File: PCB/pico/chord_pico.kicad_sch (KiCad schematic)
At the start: 83 parts, among them SW1 SW_DIP_x01, SW2 SW_DIP_x01, U1 PiPico, U2 ADG706BRUZ, U6 LM4040DBZ-3, U7 TPS7A2042

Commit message: PCB progress 60%
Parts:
- removed JP2: Bypass, Jumper:SolderJumper-2_P1.3mm_Open_RoundedPad1.0x1.5mm, symbol Jumper:SolderJumper_2_Open
- added C19, C20, C21, C22, C23, C24, C25, C26, C27, C28: 0.1uF, Capacitor_SMD:C_0603_1608Metric_Pad1.08x0.95mm_HandSolder, symbol Device:C
- renumbered C19 to CC1, C20 to CC2, H4 to H1, H6 to H2, H2 to H4, H1 to H5, H5 to H6
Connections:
- net V1 is gone; now on net Vref: C8.1
- net V2 is gone; now on net Vref: C9.1
- net +5V: now also C19.1, C20.1, C21.1, C22.1, C23.1, C24.1, C25.1, C26.1, C27.1, C28.1; no longer C10.1, C11.1, C12.1, C13.1, C14.1, C15.1, C16.1
- net AUX1: now also U1.19 (GPIO14); no longer U1.1 (GPIO0)
- net AUX2: now also U1.20 (GPIO15); no longer U1.2 (GPIO1)
- net F1: now also U2.25 (S7); no longer U2.7 (S13)
- net F2: now also U2.26 (S8)
- net F3: now also U2.4 (S16); no longer U2.5 (S15)
- net F4: now also U2.5 (S15)
- net GND: now also H13.3 (G), H14.3 (G), H15.3 (G), H16.3 (G), SW1.2, SW2.2, C19.2, C20.2, C21.2, C22.2, C23.2, C24.2, C25.2, C26.2, C27.2, C28.2
- net K1: now also H1.2 (OUT), U2.24 (S6); no longer H6.2 (OUT), U2.19 (S1)
- net K10: now also U2.8 (S12); no longer U2.10 (S10)
- net K11: now also U2.7 (S13); no longer U2.9 (S11)
- net K12: now also U2.6 (S14); no longer U2.8 (S12)
- net K2: now also H2.2 (OUT), U2.23 (S5); no longer H5.2 (OUT), U2.20 (S2)
- net K3: now also H3.2 (OUT), U2.22 (S4); no longer H4.2 (OUT), U2.21 (S3)
- net K4: now also H4.2 (OUT), U2.21 (S3); no longer H3.2 (OUT), U2.22 (S4)
- net K5: now also H5.2 (OUT), U2.20 (S2); no longer H2.2 (OUT), U2.23 (S5)
- net K6: now also H6.2 (OUT), U2.19 (S1); no longer H1.2 (OUT), U2.24 (S6)
- net K7: now also U2.11 (S9); no longer U2.25 (S7)
- net K8: now also U2.10 (S10); no longer U2.26 (S8)
- net K9: now also U2.9 (S11); no longer U2.11 (S9)
- net Vref: now also C10.1, C11.1, C12.1, C13.1, C14.1, C15.1, C16.1
- net at D1.I (In), D13.I (In), D14.I (In)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: now also U1.1 (GPIO0); no longer U1.17 (GPIO13)
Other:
- moved on the sheet: C1, C2, C3, C4, C5, C6, C7, CC1, CC2, D1, D10, D11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

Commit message: PCB v1.0
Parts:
- added CC3: 0.1uF, Capacitor_SMD:C_0603_1608Metric_Pad1.08x0.95mm_HandSolder, symbol Device:C
- R4: value 10K -> 5.1K
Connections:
- net GND: now also CC3.2
- net Vref: now also CC3.1
- net at U1.22 (GPIO17): now also U2.14 (A3); no longer U2.18 (EN)
- net at U1.24 (GPIO18): now also U2.15 (A2); no longer U2.14 (A3)
- net at U1.25 (GPIO19): now also U2.16 (A1); no longer U2.15 (A2)
- net at U1.26 (GPIO20): now also U2.17 (A0); no longer U2.16 (A1)
- net at U1.27 (GPIO21): now also U2.18 (EN); no longer U2.17 (A0)
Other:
- moved on the sheet: R3, Z1

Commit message: PCB v1.11
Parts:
- removed C13, C14, C15, C16: 0.1uF, Capacitor_SMD:C_0603_1608Metric_Pad1.08x0.95mm_HandSolder, symbol Device:C
- removed H13, H14, H15, H16: SS49E_SOT23, Package_TO_SOT_THT:TO-92Flat, symbol nos_plus:SS49E_SOT23
- added C29, C30, C31, C32: 0.1uF, Capacitor_SMD:C_0603_1608Metric_Pad1.08x0.95mm_HandSolder, symbol Device:C
- added D35, D36, D37, D38, D39, D40, D41, D42: WS2812B_Unified, chord_pico:WS2812B-2835, symbol chord_pico:WS2812B_Unified
- added IR1, IR10, IR2, IR3, IR4, IR5, IR6, IR7, IR8, IR9: ITR1502, chord_pico:ITR1502, symbol chord_pico:ITR1502
- added R10, R12, R14, R16, R18, R20, R22, R24, R6, R8: 10K, Resistor_SMD:R_0603_1608Metric_Pad0.98x0.95mm_HandSolder, symbol Device:R
- added R11, R13, R15, R17, R19, R21, R23, R5, R7, R9: 200, Resistor_SMD:R_0603_1608Metric_Pad0.98x0.95mm_HandSolder, symbol Device:R
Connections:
- net +5V: now also C29.1, C30.1, C31.1, C32.1, D35.V (VDD), D36.V (VDD), D37.V (VDD), D38.V (VDD), D39.V (VDD), D40.V (VDD), D41.V (VDD), D42.V (VDD)
- net F1: now also U1.4 (GPIO2), IR1.1, R6.2; no longer U2.25 (S7)
- net F2: now also U1.5 (GPIO3), IR2.1, R8.2; no longer U2.26 (S8)
- net F3: now also U1.6 (GPIO4), IR3.1, R10.2; no longer U2.4 (S16)
- net F4: now also U1.7 (GPIO5), IR4.1, R12.2; no longer U2.5 (S15)
- net GND: now also C29.2, C30.2, C31.2, C32.2, D35.G (VSS), D36.G (VSS), D37.G (VSS), D38.G (VSS), D39.G (VSS), D40.G (VSS), D41.G (VSS), D42.G (VSS), R10.1, R11.1, R12.1, R13.1, R14.1, R15.1, R16.1, R17.1, R18.1, R19.1, R20.1, R21.1, R22.1, R23.1, R24.1, R5.1, R6.1, R7.1, R8.1, R9.1
- net F6: now reaches U1.10 (GPIO7)
- net F6: now also IR6.1, R16.2
- net F7: now reaches U1.11 (GPIO8)
- net F7: now also IR7.1, R18.2
- net F8: now reaches U1.12 (GPIO9)
- net F8: now also IR8.1, R20.2
- net F9: now reaches U1.14 (GPIO10)
- net F9: now also IR9.1, R22.2
- net F10: now reaches U1.15 (GPIO11)
- net F10: now also IR10.1, R24.2
- net at U1.2 (GPIO1): now also D35.I (In), D39.I (In)
- net +3.3V: now reaches U1.36 (3V3)
- net +3.3V: now also IR1.2, IR1.4 (A), IR10.2, IR10.4 (A), IR2.2, IR2.4 (A), IR3.2, IR3.4 (A), IR4.2, IR4.4 (A), IR5.2, IR5.4 (A), IR6.2, IR6.4 (A), IR7.2, IR7.4 (A), IR8.2, IR8.4 (A), IR9.2, IR9.4 (A)
- net F5: now reaches U1.9 (GPIO6)
- net F5: now also IR5.1, R14.2
- new net: D36.O (Out), D37.I (In), D41.I (In)
- new net: D37.O (Out), D38.I (In), D42.I (In)
- new net: IR6.3 (K), R15.2
- new net: D35.O (Out), D36.I (In), D40.I (In)
- new net: IR5.3 (K), R13.2
- new net: IR7.3 (K), R17.2
- new net: IR8.3 (K), R19.2
- new net: IR2.3 (K), R7.2
- new net: IR4.3 (K), R11.2
- new net: IR10.3 (K), R23.2
- new net: IR1.3 (K), R5.2
- new net: IR3.3 (K), R9.2
- new net: IR9.3 (K), R21.2
- no-connect marks 41 -> 36
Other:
- moved on the sheet: CC3, D1, D10, D11, D12, D13, D14, D15, D16, D17, D18, D19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

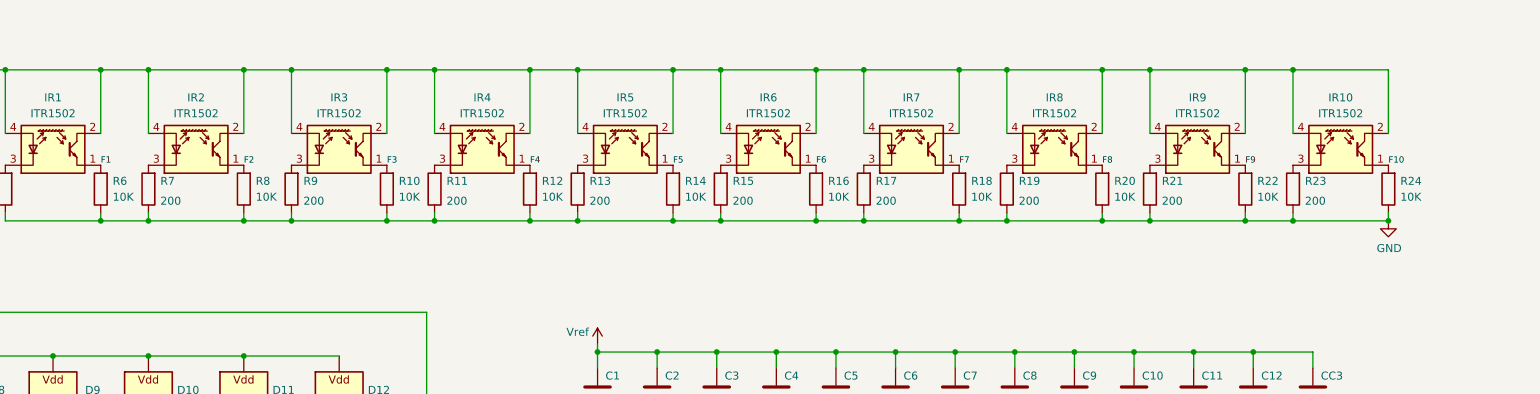
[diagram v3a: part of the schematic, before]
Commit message: PCB v1.2 (correct values and signature)
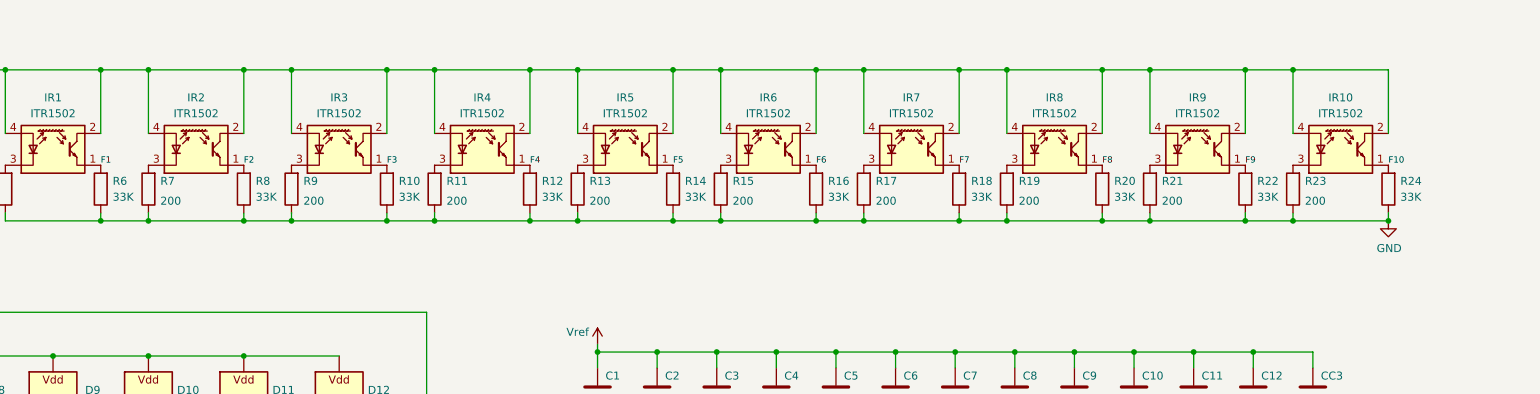
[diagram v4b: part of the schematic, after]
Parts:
- R10, R12, R14, R16, R18, R20, R22, R24, R6, R8: value 10K -> 33K
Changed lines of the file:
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@@
 			)
 		)
-		(property "Value" "10K"
+		(property "Value" "33K"
 			(at 216.535 170.815 0)
 			(effects
@@
 			)
 		)
-		(property "Value" "10K"
+		(property "Value" "33K"
 			(at 239.395 170.815 0)
 			(effects
@@
 			)
 		)
-		(property "Value" "10K"
+		(property "Value" "33K"
 			(at 330.835 170.815 0)
 			(effects
@@
 			)
 		)
-		(property "Value" "10K"
+		(property "Value" "33K"
 			(at 376.555 170.815 0)
 			(effects
@@
 			)
 		)
-		(property "Value" "10K"
+		(property "Value" "33K"
 			(at 353.695 170.815 0)
 			(effects
@@
 			)
 		)
-		(property "Value" "10K"
+		(property "Value" "33K"
 			(at 262.255 170.815 0)
 			(effects
@@
 			)
 		)
-		(property "Value" "10K"
+		(property "Value" "33K"
 			(at 193.675 170.815 0)
 			(effects
@@
 			)
 		)
-		(property "Value" "10K"
+		(property "Value" "33K"
 			(at 285.115 170.815 0)
 			(effects
@@
 			)
 		)
-		(property "Value" "10K"
+		(property "Value" "33K"
 			(at 170.815 170.815 0)
 			(effects
@@
 			)
 		)
-		(property "Value" "10K"
+		(property "Value" "33K"
 			(at 307.975 170.815 0)
 			(effects

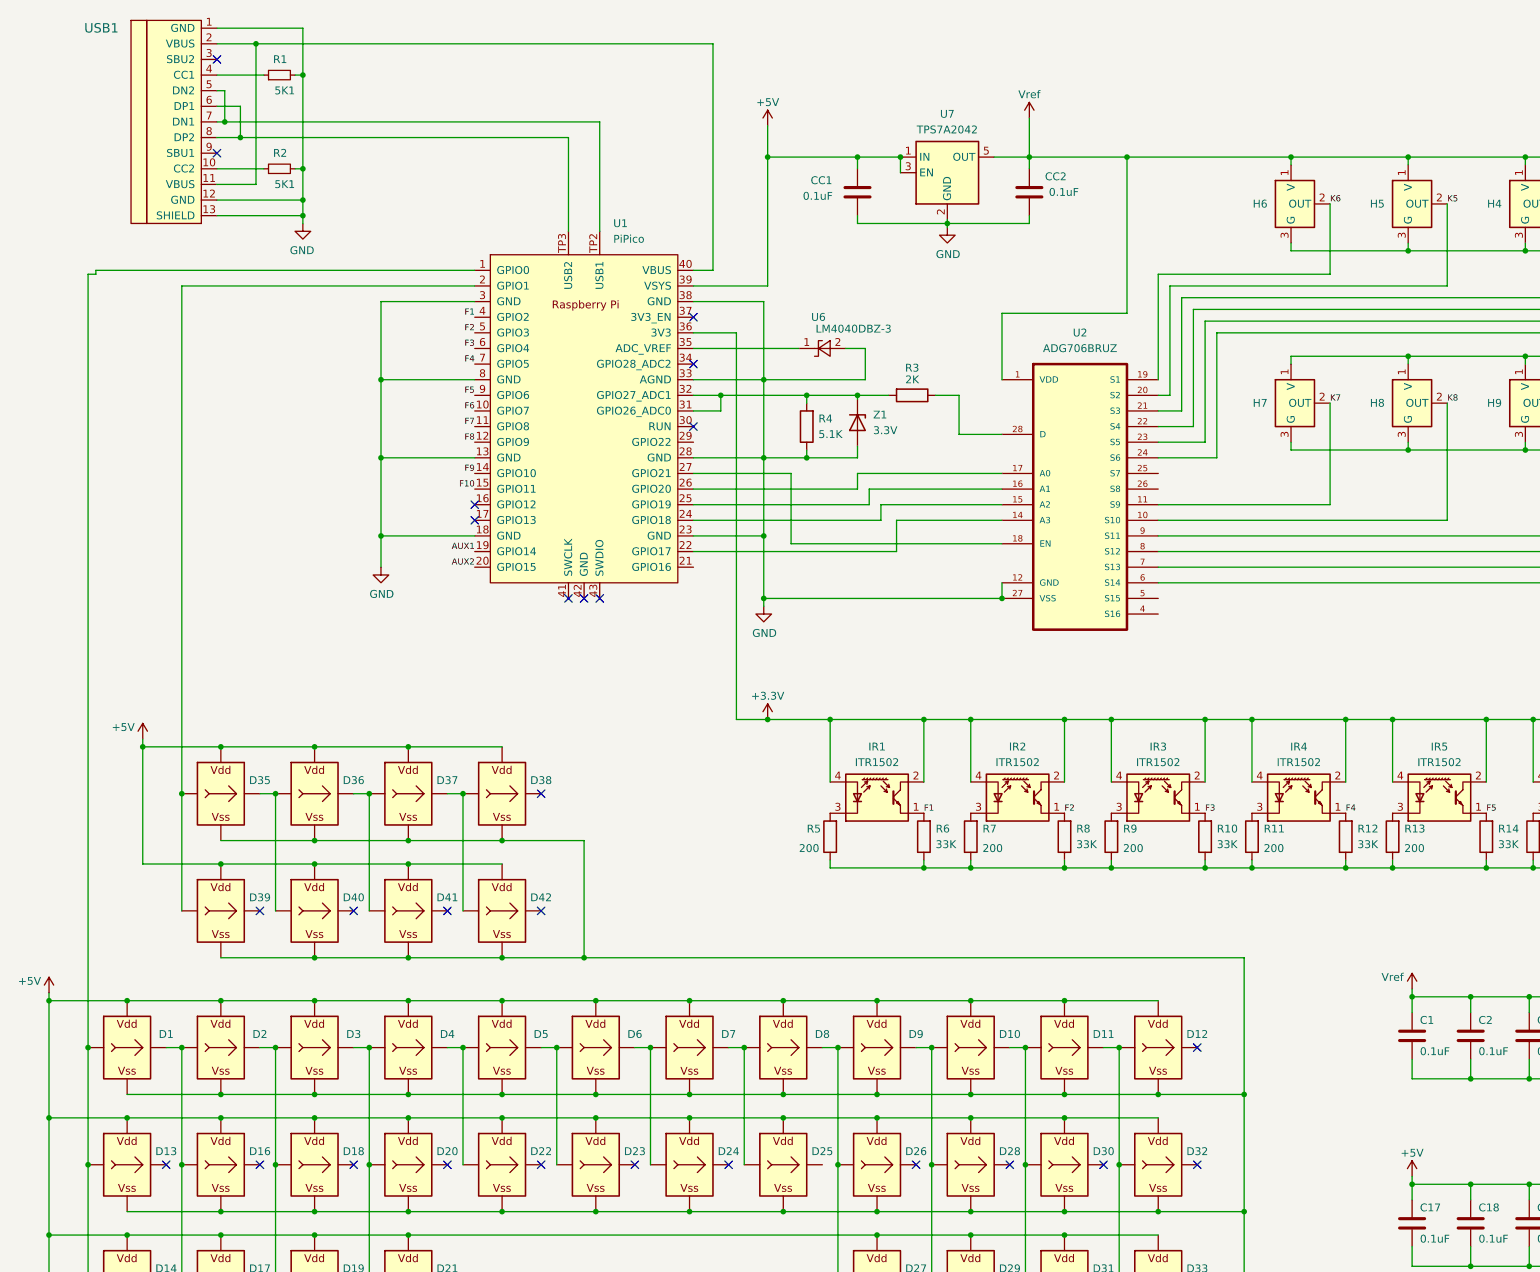
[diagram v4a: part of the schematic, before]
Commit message: PCB optimization, VBUS for LDO
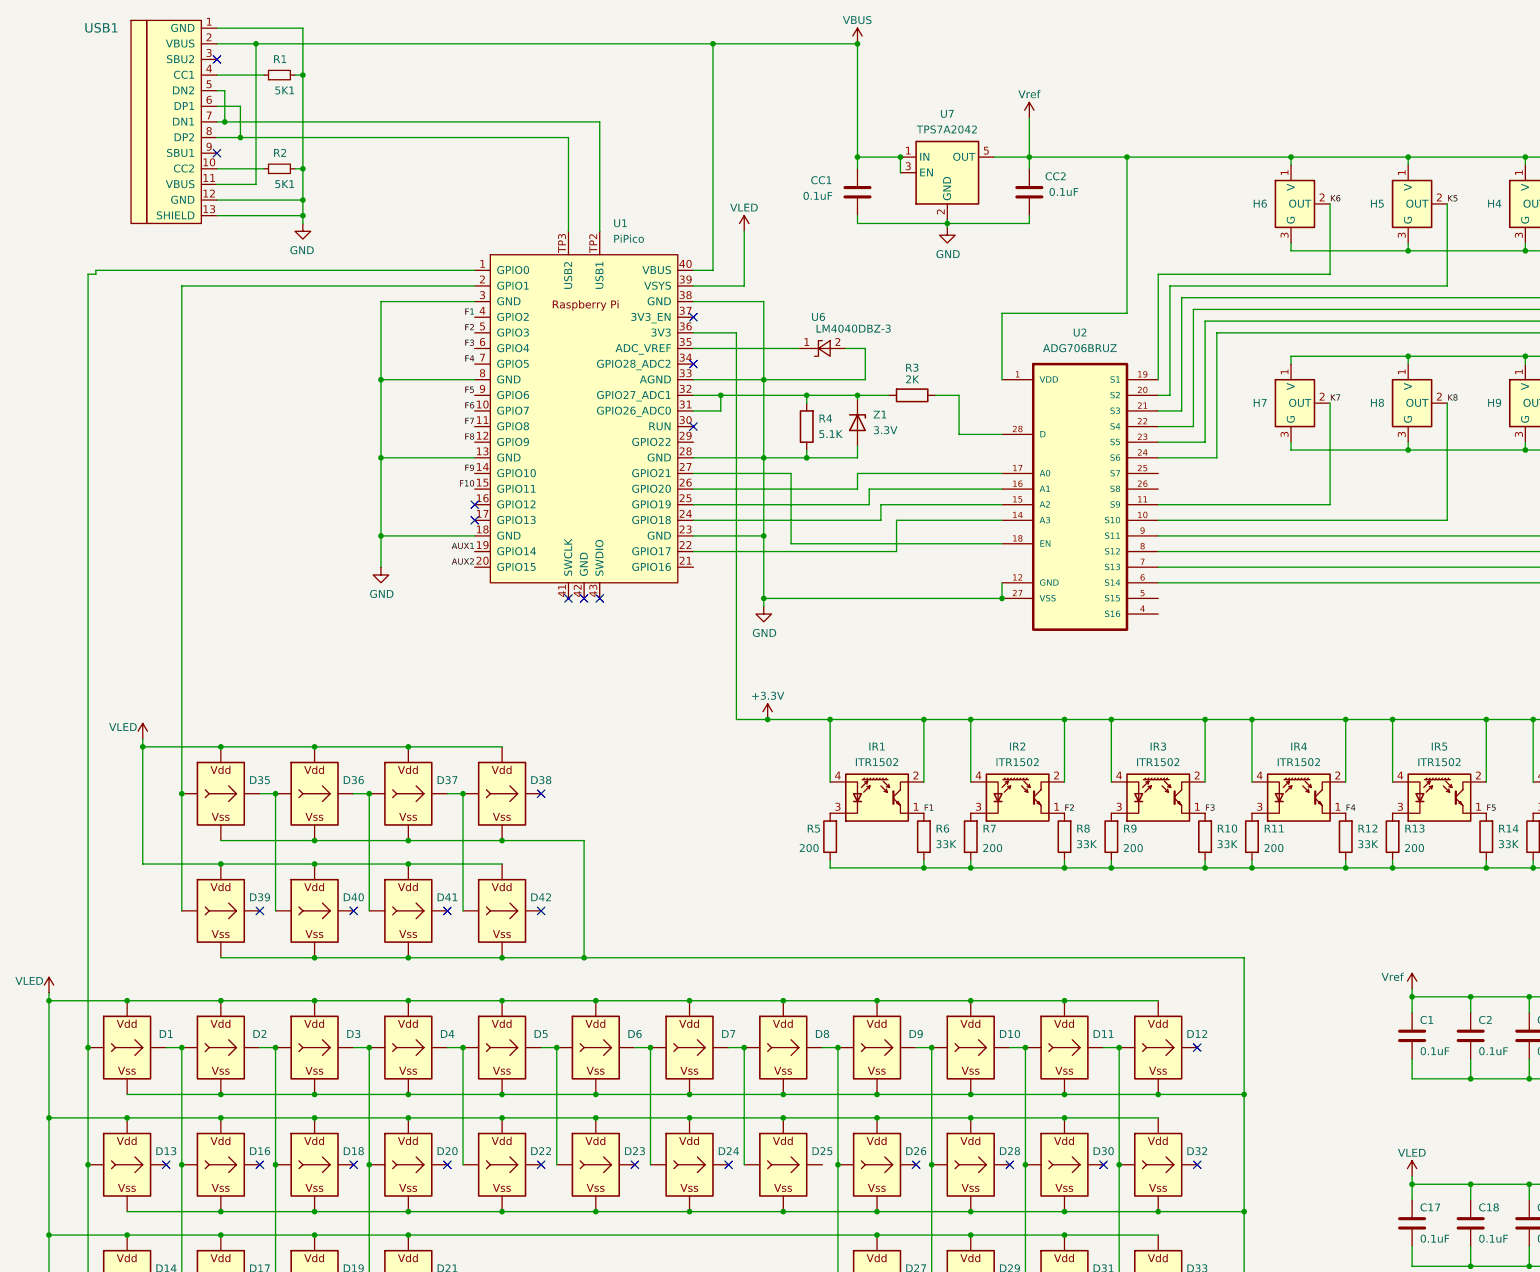
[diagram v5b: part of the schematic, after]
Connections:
- net VBUS: now reaches U1.40 (VBUS), USB1.11 (VBUS), USB1.2 (VBUS)
- net VBUS: now also CC1.1, U7.1 (IN), U7.3 (EN)
- net +5V renamed VLED
- net VLED: no longer CC1.1, U7.1 (IN), U7.3 (EN)
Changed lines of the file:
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@@
 	)
 	(junction
-		(at 143.51 59.055)
-		(diameter 0)
-		(color 0 0 0 0)
-	)
-	(junction
 		(at 295.91 208.915)
 		(diameter 0)
@@
 	)
 	(junction
+		(at 134.62 40.64)
+		(diameter 0)
+		(color 0 0 0 0)
+	)
+	(junction
 		(at 165.1 59.055)
 		(diameter 0)
@@
 	)
 	(junction
-		(at 158.115 59.055)
-		(diameter 0)
-		(color 0 0 0 0)
-	)
-	(junction
 		(at 336.55 150.495)
 		(diameter 0)
@@
 	)
 	(junction
+		(at 158.115 59.055)
+		(diameter 0)
+		(color 0 0 0 0)
+	)
+	(junction
 		(at 100.33 189.23)
 		(diameter 0)
@@
 	)
 	(junction
+		(at 158.115 40.64)
+		(diameter 0)
+		(color 0 0 0 0)
+	)
+	(junction
 		(at 248.285 226.06)
 		(diameter 0)
@@
 	(wire
 		(pts
-			(xy 143.51 59.055) (xy 158.115 59.055)
-		)
-		(stroke
-			(width 0)
-			(type default)
-		)
-	)
-	(wire
-		(pts
 			(xy 237.49 174.625) (xy 245.11 174.625)
 		)
@@
 	(wire
 		(pts
-			(xy 143.51 59.055) (xy 143.51 53.975)
+			(xy 139.7 71.12) (xy 139.7 80.01)
 		)
 		(stroke
@@
 	(wire
 		(pts
+			(xy 134.62 40.64) (xy 158.115 40.64)
+		)
+		(stroke
+			(width 0)
+			(type default)
+		)
+	)
+	(wire
+		(pts
 			(xy 266.7 106.68) (xy 285.75 106.68)
 		)
@@
 	(wire
 		(pts
-			(xy 305.435 239.395) (xy 314.96 239.395)
+			(xy 158.115 40.64) (xy 158.115 59.055)
 		)
 		(stroke
@@
 	(wire
 		(pts
-			(xy 91.44 162.56) (xy 93.98 162.56)
+			(xy 305.435 239.395) (xy 314.96 239.395)
 		)
 		(stroke
@@
 	(wire
 		(pts
-			(xy 54.61 154.94) (xy 69.85 154.94)
+			(xy 91.44 162.56) (xy 93.98 162.56)
 		)
 		(stroke
@@
 	(wire
 		(pts
-			(xy 347.345 59.055) (xy 347.345 91.44)
+			(xy 54.61 154.94) (xy 69.85 154.94)
 		)
 		(stroke
-			(width 0.254)
+			(width 0)
 			(type default)
 		)
@@
 	(wire
 		(pts
-			(xy 186.055 59.055) (xy 186.055 60.96)
+			(xy 347.345 59.055) (xy 347.345 91.44)
 		)
 		(stroke
@@
 	(wire
 		(pts
-			(xy 176.53 150.495) (xy 191.77 150.495)
+			(xy 186.055 59.055) (xy 186.055 60.96)
 		)
 		(stroke
-			(width 0)
+			(width 0.254)
 			(type default)
 		)
@@
 	(wire
 		(pts
-			(xy 143.51 80.01) (xy 143.51 59.055)
+			(xy 176.53 150.495) (xy 191.77 150.495)
 		)
 		(stroke
@@
 	(wire
 		(pts
-			(xy 131.445 80.01) (xy 143.51 80.01)
+			(xy 131.445 80.01) (xy 139.7 80.01)
 		)
 		(stroke
@@
 	)
 	(symbol
+		(lib_id "power:+5V")
+		(at 158.115 40.64 0)
+		(unit 1)
+		(exclude_from_sim no)
+		(in_bom yes)
+		(on_board yes)
+		(dnp no)
+		(property "Reference" "#PWR04"
+			(at 158.115 44.45 0)
+			(effects
+				(font
+					(size 1.27 1.27)
+				)
+				(hide yes)
+			)
+		)
+		(property "Value" "VBUS"
+			(at 158.115 36.83 0)
+			(effects
+				(font
+					(size 1.27 1.27)
+				)
+			)
+		)
+		(property "Footprint" ""
+			(at 158.115 40.64 0)
+			(effects
+				(font
+					(size 1.27 1.27)
+				)
+				(hide yes)
+			)
+		)
+		(property "Datasheet" ""
+			(at 158.115 40.64 0)
+			(effects
+				(font
+					(size 1.27 1.27)
+				)
+				(hide yes)
+			)
+		)
+		(property "Description" "Power symbol creates a global label with name \"+5V\""
+			(at 158.115 40.64 0)
+			(effects
+				(font
+					(size 1.27 1.27)
+				)
+				(hide yes)
+			)
+		)
+		(pin "1"
+		)
+		(instances
+			(project "chord_pico"
+				(path "/2e3f5573-c264-4a8b-a2f0-0e6473d39aad"
+					(reference "#PWR04")
+					(unit 1)
+				)
+			)
+		)
+	)
+	(symbol
 		(lib_id "chord_pico:WS2812B_Unified")
 		(at 85.09 222.885 0)
@@
 			)
 		)
-		(property "Value" "+5V"
+		(property "Value" "VLED"
 			(at 248.285 220.98 0)
 			(effects
@@
 	(symbol
 		(lib_id "power:+5V")
-		(at 143.51 53.975 0)
+		(at 139.7 71.12 0)
 		(unit 1)
 		(exclude_from_sim no)
@@
 		(dnp no)
 		(property "Reference" "#PWR01"
-			(at 143.51 57.785 0)
+			(at 139.7 74.93 0)
 			(effects
 				(font
@@
 			)
 		)
-		(property "Value" "+5V"
-			(at 143.51 50.165 0)
+		(property "Value" "VLED"
+			(at 139.7 67.31 0)
 			(effects
 				(font
@@
 		)
 		(property "Footprint" ""
-			(at 143.51 53.975 0)
+			(at 139.7 71.12 0)
 			(effects
 				(font
@@
 		)
 		(property "Datasheet" ""
-			(at 143.51 53.975 0)
+			(at 139.7 71.12 0)
 			(effects
 				(font
@@
 		)
 		(property "Description" "Power symbol creates a global label with name \"+5V\""
-			(at 143.51 53.975 0)
+			(at 139.7 71.12 0)
 			(effects
 				(font
@@
 			)
 		)
-		(property "Value" "+5V"
+		(property "Value" "VLED"
 			(at 38.735 151.765 0)
 			(effects
@@
 			)
 		)
-		(property "Value" "+5V"
+		(property "Value" "VLED"
 			(at 23.495 193.04 0)
 			(effects
